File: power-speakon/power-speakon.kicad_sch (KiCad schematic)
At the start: 11 parts, among them J101 NL4MDXX-V-3, J102 NL4MDXX-V-3, J103 WAGO 2601-1101, J104 WAGO 2601-1101

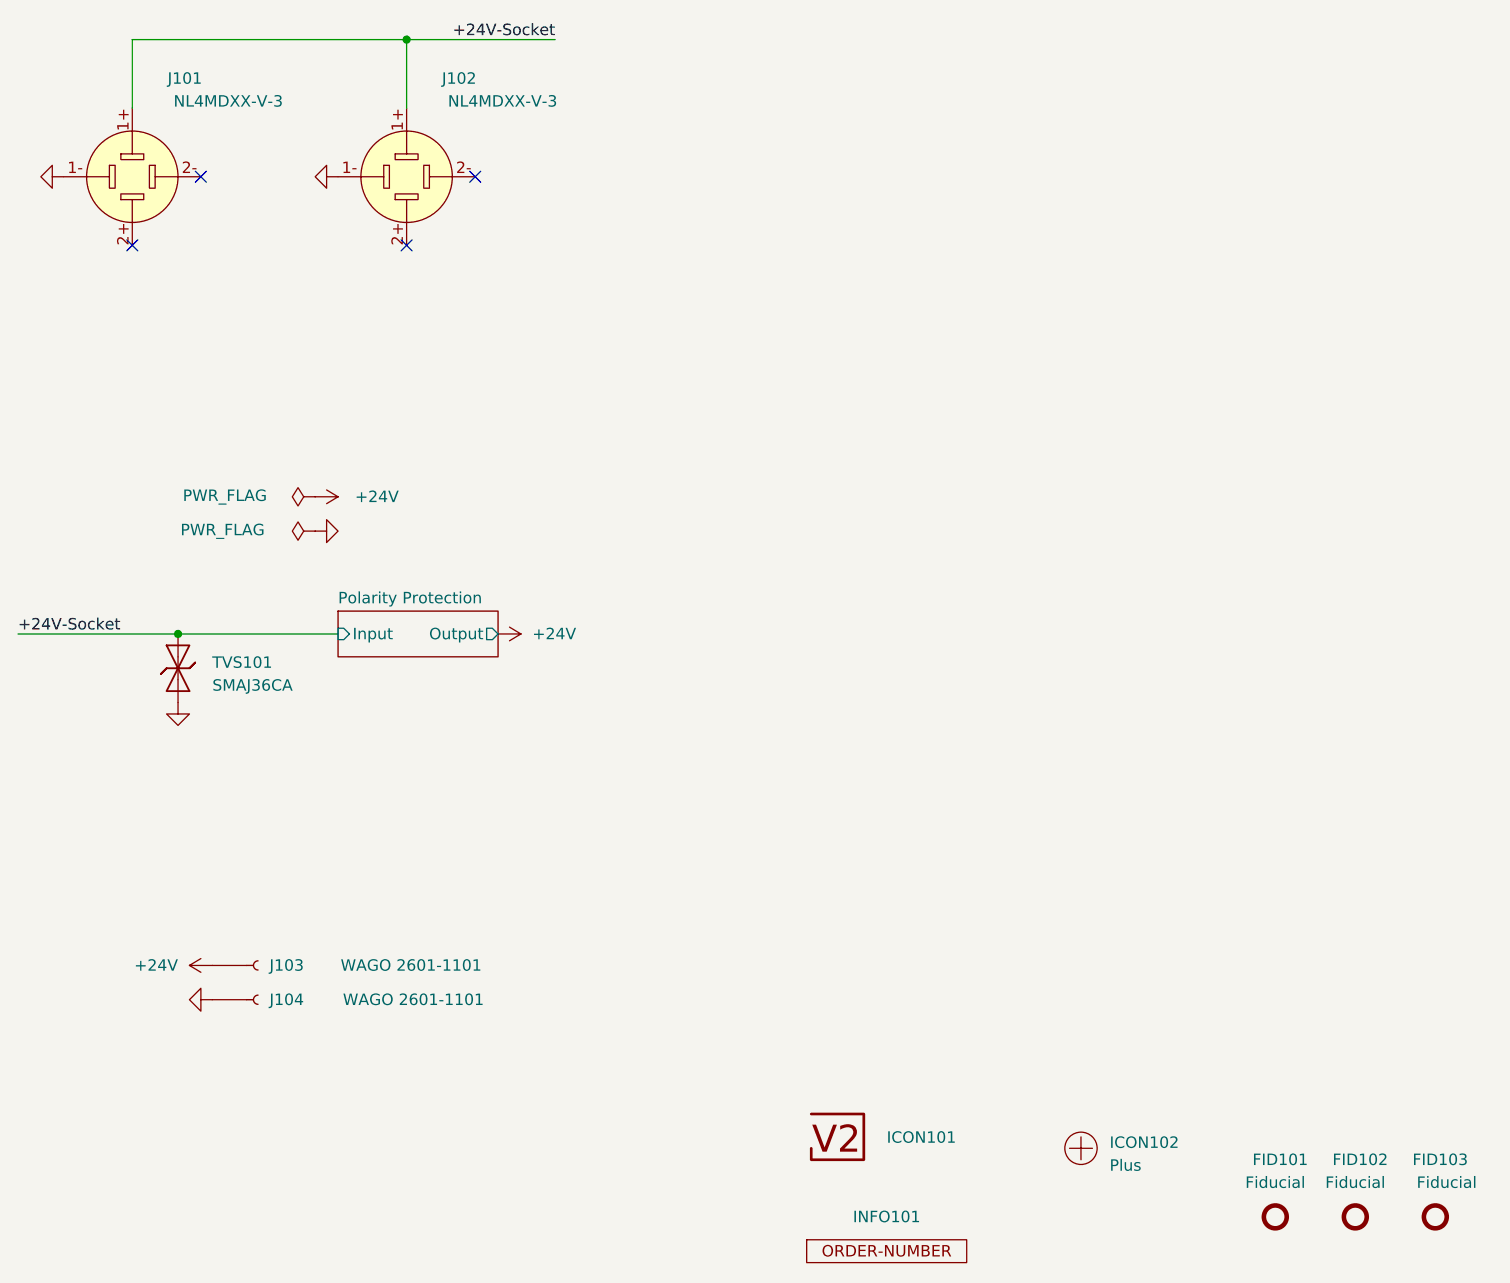
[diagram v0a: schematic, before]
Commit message: Update power symbols
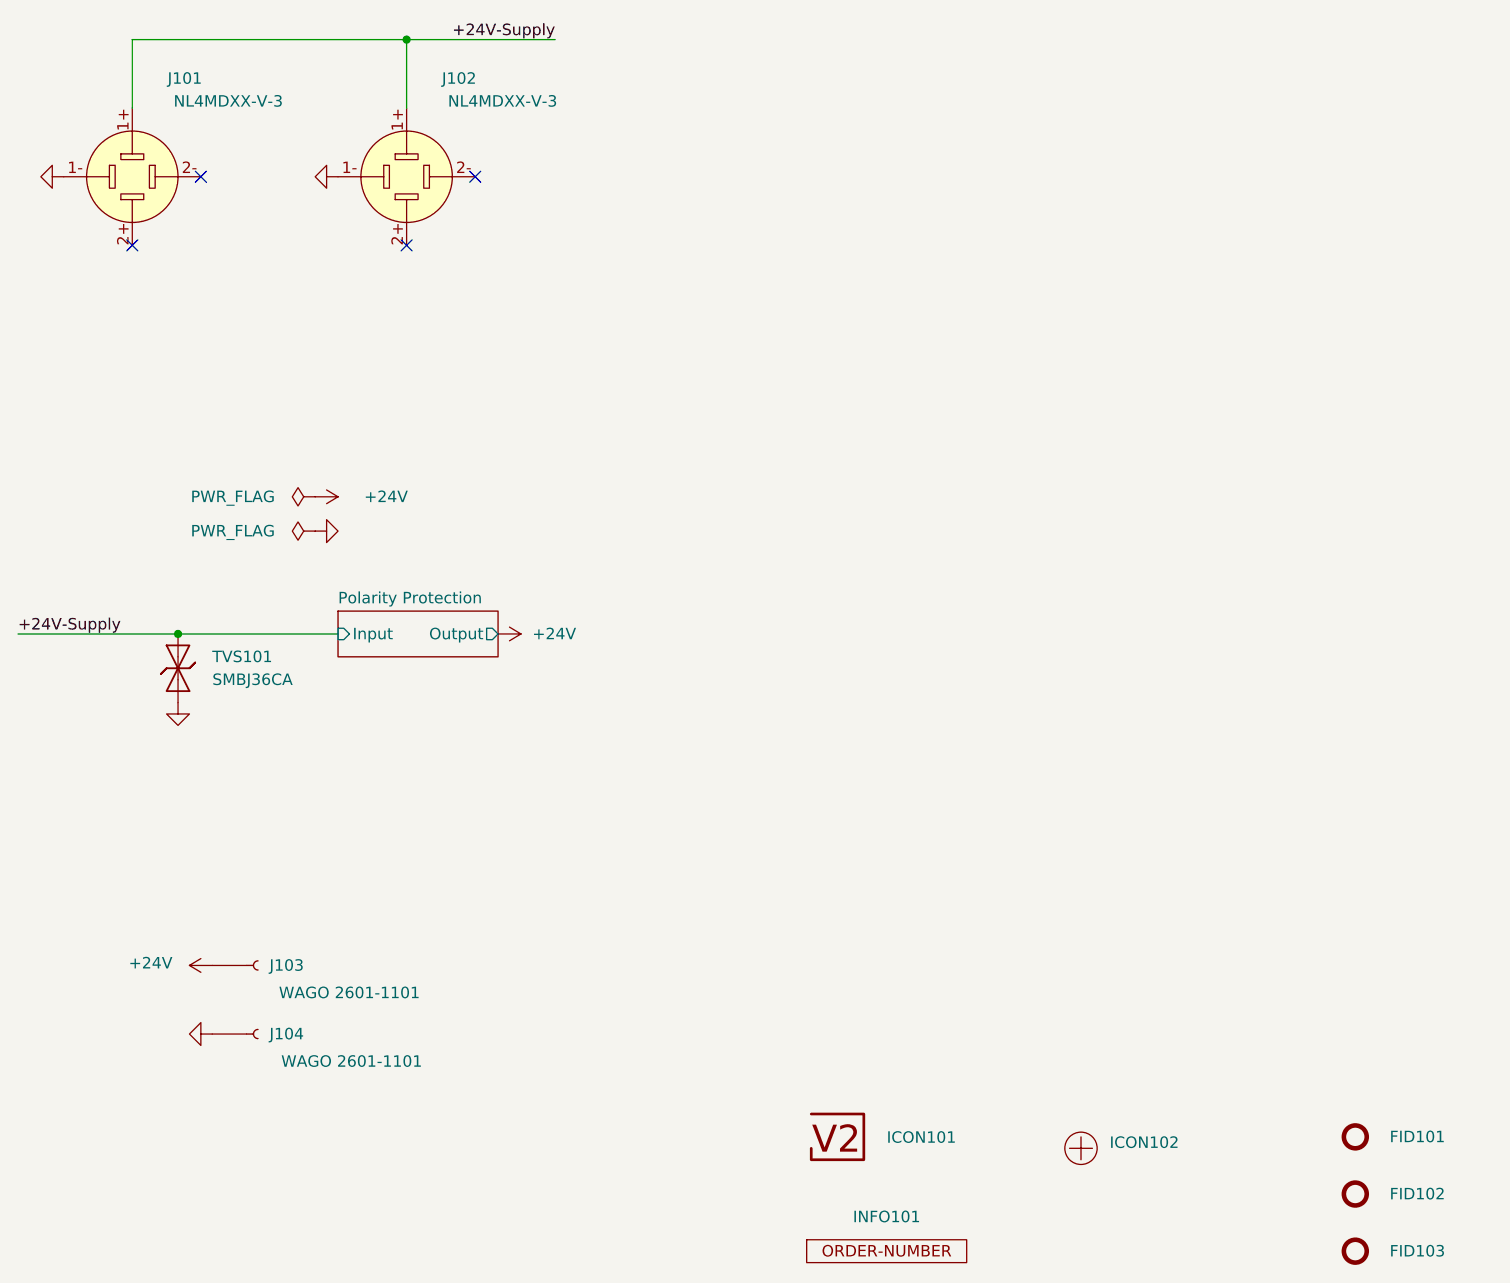
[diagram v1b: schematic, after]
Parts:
- FID101, FID102, FID103: value Fiducial -> Fiducial_Paste
- INFO101: value ORDER-NUMBER -> Order_Number
- J101, J102: Mouser (none) -> 568-NL4MDXXV3
- TVS101: value SMAJ36CA -> SMBJ36CA; footprint Diode_SMD:D_SMA -> V2_Diode_SMD:D_SMB; symbol V2_Diode:SMAJ36CA -> V2_Diode:SMBJ36CA; Mouser (none) -> 652-SMBJ36CA-Q
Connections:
- net +24V-Socket renamed +24V-Supply
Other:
- moved on the sheet: FID101, FID102, FID103, J104

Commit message: Update parts
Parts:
- J101, J102: Manufacturer (none) -> Neutrik; Product (none) -> NL4MDXXV3
- J103, J104: Manufacturer (none) -> WAGO; Product (none) -> 2601-1101
- TVS101: Manufacturer (none) -> Bourns; Product (none) -> SMBJ36CA-Q; Rating (none) -> 36V
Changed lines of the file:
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@@
+			)
+		)
+		(property "Product" "SMBJ36CA-Q"
+			(at 146.05 114.3 0)
+			(effects
+				(font
+					(size 1.27 1.27)
+				)
+				(hide yes)
+			)
+		)
+		(property "Manufacturer" "Bourns"
+			(at 143.51 114.3 0)
+			(effects
+				(font
+					(size 1.27 1.27)
+				)
+				(hide yes)
+			)
+		)
+		(property "Rating" "36V"
+			(at 148.59 114.3 0)
+			(effects
+				(font
+					(size 1.27 1.27)
+				)
+				(hide yes)
+			)
+		)
+		(property "Sim.Enable" ""
+			(at 135.89 114.3 90)
+			(effects
+				(font
+					(size 1.27 1.27)
+				)
+				(hide yes)
 			)
 		)
@@
 		(at 209.55 166.37 0)
 		(unit 1)
-		(exclude_from_sim no)
+		(exclude_from_sim yes)
 		(in_bom no)
 		(on_board yes)
@@
 			)
 		)
-		(property "Sim.Enable" "0"
+		(property "Sim.Enable" ""
 			(at 209.55 166.37 0)
 			(effects
@@
 			)
 		)
+		(property "Manufacturer" "WAGO"
+			(at 144.78 158.75 0)
+			(effects
+				(font
+					(size 1.27 1.27)
+				)
+				(hide yes)
+			)
+		)
+		(property "Product" "2601-1101"
+			(at 144.78 161.798 0)
+			(effects
+				(font
+					(size 1.27 1.27)
+				)
+				(hide yes)
+			)
+		)
+		(property "Sim.Enable" ""
+			(at 144.78 147.32 0)
+			(effects
+				(font
+					(size 1.27 1.27)
+				)
+				(hide yes)
+			)
+		)
 		(pin "1"
 		)
@@
 		(at 236.22 167.64 0)
 		(unit 1)
-		(exclude_from_sim no)
+		(exclude_from_sim yes)
 		(in_bom no)
 		(on_board yes)
@@
 			)
 		)
-		(property "Sim.Enable" "0"
+		(property "Sim.Enable" ""
 			(at 236.22 167.64 0)
 			(effects
@@
 			)
 		)
+		(property "Manufacturer" "Neutrik"
+			(at 161.29 87.63 0)
+			(effects
+				(font
+					(size 1.27 1.27)
+				)
+				(hide yes)
+			)
+		)
+		(property "Product" "NL4MDXXV3"
+			(at 161.29 90.17 0)
+			(effects
+				(font
+					(size 1.27 1.27)
+				)
+				(hide yes)
+			)
+		)
+		(property "Sim.Enable" ""
+			(at 161.29 59.69 0)
+			(effects
+				(font
+					(size 1.27 1.27)
+				)
+				(hide yes)
+			)
+		)
 		(pin "2-"
 		)
@@
 			)
 		)
+		(property "Sim.Enable" ""
+			(at 214.63 179.07 0)
+			(effects
+				(font
+					(size 1.27 1.27)
+				)
+				(hide yes)
+			)
+		)
 		(instances
 			(project "cube-cover"
@@
 			)
 		)
+		(property "Manufacturer" "WAGO"
+			(at 144.78 166.37 0)
+			(effects
+				(font
+					(size 1.27 1.27)
+				)
+				(hide yes)
+			)
+		)
+		(property "Product" "2601-1101"
+			(at 144.78 169.418 0)
+			(effects
+				(font
+					(size 1.27 1.27)
+				)
+				(hide yes)
+			)
+		)
+		(property "Sim.Enable" ""
+			(at 144.78 154.94 0)
+			(effects
+				(font
+					(size 1.27 1.27)
+				)
+				(hide yes)
+			)
+		)
 		(pin "1"
 		)
@@
 			)
 		)
+		(property "Sim.Enable" ""
+			(at 266.7 166.37 0)
+			(effects
+				(font
+					(size 1.27 1.27)
+				)
+				(hide yes)
+			)
+		)
 		(instances
 			(project "power-speakon"
@@
 			)
 		)
+		(property "Manufacturer" "Neutrik"
+			(at 130.81 87.63 0)
+			(effects
+				(font
+					(size 1.27 1.27)
+				)
+				(hide yes)
+			)
+		)
+		(property "Product" "NL4MDXXV3"
+			(at 130.81 90.17 0)
+			(effects
+				(font
+					(size 1.27 1.27)
+				)
+				(hide yes)
+			)
+		)
+		(property "Sim.Enable" ""
+			(at 130.81 59.69 0)
+			(effects
+				(font
+					(size 1.27 1.27)
+				)
+				(hide yes)
+			)
+		)
 		(pin "2-"
 		)
@@
 			)
 		)
+		(property "Sim.Enable" ""
+			(at 266.7 179.07 0)
+			(effects
+				(font
+					(size 1.27 1.27)
+				)
+				(hide yes)
+			)
+		)
 		(instances
 			(project "power-speakon"
@@
 			(at 266.7 172.72 0)
 			(effects
+				(font
+					(size 1.27 1.27)
+				)
+				(hide yes)
+			)
+		)
+		(property "Sim.Enable" ""
+			(at 266.7 172.72 0)
+			(effects

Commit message: Refresh
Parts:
- J101, J102: footprint V2_Connector_Audio:Jack_speakON_Neutrik_NL4MDXX-V-3_Vertical -> V2_Connector_SpeakOn:Jack_speakON_Neutrik_NL4MDXX-V-3_Vertical; symbol V2_Connector_Audio:NL4MDXX-V-3 -> V2_Connector_SpeakOn:NL4MDXX-V-3
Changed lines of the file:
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@@
-			)
-		)
-		(property "Sim.Enable" ""
-			(at 135.89 114.3 90)
-			(effects
-				(font
-					(size 1.27 1.27)
-				)
-				(hide yes)
 			)
 		)
@@
 		(at 209.55 166.37 0)
 		(unit 1)
-		(exclude_from_sim yes)
+		(exclude_from_sim no)
 		(in_bom no)
 		(on_board yes)
@@
 			)
 		)
-		(property "Sim.Enable" ""
+		(property "Sim.Enable" "0"
 			(at 209.55 166.37 0)
 			(effects
@@
 			)
 		)
-		(property "Sim.Enable" ""
-			(at 144.78 147.32 0)
-			(effects
-				(font
-					(size 1.27 1.27)
-				)
-				(hide yes)
-			)
-		)
 		(pin "1"
 		)
@@
 		(at 236.22 167.64 0)
 		(unit 1)
-		(exclude_from_sim yes)
+		(exclude_from_sim no)
 		(in_bom no)
 		(on_board yes)
@@
 			)
 		)
-		(property "Sim.Enable" ""
+		(property "Sim.Enable" "0"
 			(at 236.22 167.64 0)
 			(effects
@@
 	)
 	(symbol
-		(lib_id "V2_Connector_Audio:NL4MDXX-V-3")
+		(lib_id "V2_Connector_SpeakOn:NL4MDXX-V-3")
 		(at 161.29 59.69 0)
 		(unit 1)
@@
 			)
 		)
-		(property "Footprint" "V2_Connector_Audio:Jack_speakON_Neutrik_NL4MDXX-V-3_Vertical"
+		(property "Footprint" "V2_Connector_SpeakOn:Jack_speakON_Neutrik_NL4MDXX-V-3_Vertical"
 			(at 161.29 59.69 0)
 			(effects
@@
 			)
 		)
-		(property "Sim.Enable" ""
-			(at 161.29 59.69 0)
-			(effects
-				(font
-					(size 1.27 1.27)
-				)
-				(hide yes)
-			)
-		)
 		(pin "2-"
 		)
@@
 			)
 		)
-		(property "Sim.Enable" ""
-			(at 214.63 179.07 0)
-			(effects
-				(font
-					(size 1.27 1.27)
-				)
-				(hide yes)
-			)
-		)
 		(instances
 			(project "cube-cover"
@@
 			)
 		)
-		(property "Sim.Enable" ""
-			(at 144.78 154.94 0)
-			(effects
-				(font
-					(size 1.27 1.27)
-				)
-				(hide yes)
-			)
-		)
 		(pin "1"
 		)
@@
 			)
 		)
-		(property "Sim.Enable" ""
-			(at 266.7 166.37 0)
-			(effects
-				(font
-					(size 1.27 1.27)
-				)
-				(hide yes)
-			)
-		)
 		(instances
 			(project "power-speakon"
@@
 	)
 	(symbol
-		(lib_id "V2_Connector_Audio:NL4MDXX-V-3")
+		(lib_id "V2_Connector_SpeakOn:NL4MDXX-V-3")
 		(at 130.81 59.69 0)
 		(unit 1)
@@
 			)
 		)
-		(property "Footprint" "V2_Connector_Audio:Jack_speakON_Neutrik_NL4MDXX-V-3_Vertical"
+		(property "Footprint" "V2_Connector_SpeakOn:Jack_speakON_Neutrik_NL4MDXX-V-3_Vertical"
 			(at 130.81 59.69 0)
 			(effects
@@
 			)
 		)
-		(property "Sim.Enable" ""
-			(at 130.81 59.69 0)
-			(effects
-				(font
-					(size 1.27 1.27)
-				)
-				(hide yes)
-			)
-		)
 		(pin "2-"
 		)
@@
 			)
 		)
-		(property "Sim.Enable" ""
-			(at 266.7 179.07 0)
-			(effects
-				(font
-					(size 1.27 1.27)
-				)
-				(hide yes)
-			)
-		)
 		(instances
 			(project "power-speakon"
@@
 			(at 266.7 172.72 0)
 			(effects
-				(font
-					(size 1.27 1.27)
-				)
-				(hide yes)
-			)
-		)
-		(property "Sim.Enable" ""
-			(at 266.7 172.72 0)
-			(effects

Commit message: Update library
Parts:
- J101, J102: footprint V2_Connector_SpeakOn:Jack_speakON_Neutrik_NL4MDXX-V-3_Vertical -> V2_Connector_SpeakOn:NL4MDXX-V-3
- TVS101: value SMBJ36CA -> SMBJ33CA; symbol V2_Diode:SMBJ36CA -> V2_Diode:SMBJ33CA; Mouser 652-SMBJ36CA-Q -> 652-SMBJ33CA-Q; Product SMBJ36CA-Q -> SMBJ33CA-Q; Rating 36V -> 33V
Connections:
- net +24V renamed +28V
- net +24V-Supply renamed +28V-Supply
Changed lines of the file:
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@@
 		)
 	)
-	(label "+24V-Supply"
+	(label "+28V-Supply"
 		(at 177.8 44.45 180)
 		(effects
@@
 		)
 	)
-	(label "+24V-Supply"
+	(label "+28V-Supply"
 		(at 118.11 110.49 0)
 		(effects
@@
 			)
 		)
-		(property "Description" "Power symbol creates a global label with name \"GND\" , ground"
+		(property "Description" ""
 			(at 143.256 59.436 0)
 			(effects
@@
 			)
 		)
-		(property "Description" "Power symbol creates a global label with name \"GND\" , ground"
+		(property "Description" ""
 			(at 135.636 128.524 0)
 			(effects
@@
 	)
 	(symbol
-		(lib_id "V2_power:+24V")
+		(lib_id "V2_power:+28V")
 		(at 171.45 110.49 270)
 		(unit 1)
@@
 			)
 		)
-		(property "Value" "+24V"
+		(property "Value" "+28V"
 			(at 175.26 110.4899 90)
 			(effects
@@
 			)
 		)
-		(property "Description" "Power symbol creates a global label with name \"+24V\""
+		(property "Description" ""
 			(at 156.718 110.49 0)
 			(effects
@@
 	)
 	(symbol
-		(lib_id "V2_Diode:SMBJ36CA")
+		(lib_id "V2_Diode:SMBJ33CA")
 		(at 135.89 114.3 90)
 		(unit 1)
@@
 			)
 		)
-		(property "Value" "SMBJ36CA"
+		(property "Value" "SMBJ33CA"
 			(at 139.7 115.5699 90)
 			(effects
@@
 		)
 		(property "Datasheet" ""
-			(at 135.89 114.3 0)
-			(effects
-				(font
-					(size 1.27 1.27)
-				)
-				(hide yes)
-			)
-		)
-		(property "Description" ""
-			(at 135.89 114.3 0)
-			(effects
-				(font
-					(size 1.27 1.27)
-				)
-				(hide yes)
-			)
-		)
-		(property "Mouser" "652-SMBJ36CA-Q"
-			(at 143.256 114.3 0)
-			(effects
-				(font
-					(size 1.27 1.27)
-				)
-				(hide yes)
-			)
-		)
-		(property "Product" "SMBJ36CA-Q"
 			(at 146.05 114.3 0)
 			(effects
@@
 			)
 		)
+		(property "Description" "Transient Voltage Suppressor Diode, Bidirectional, 36.7-40.6V"
+			(at 148.59 114.3 0)
+			(effects
+				(font
+					(size 1.27 1.27)
+				)
+				(hide yes)
+			)
+		)
+		(property "Mouser" "652-SMBJ33CA-Q"
+			(at 159.004 114.3 0)
+			(show_name yes)
+			(effects
+				(font
+					(size 1.27 1.27)
+				)
+				(hide yes)
+			)
+		)
+		(property "Product" "SMBJ33CA-Q"
+			(at 153.67 114.3 0)
+			(show_name yes)
+			(effects
+				(font
+					(size 1.27 1.27)
+				)
+				(hide yes)
+			)
+		)
 		(property "Manufacturer" "Bourns"
-			(at 143.51 114.3 0)
-			(effects
-				(font
-					(size 1.27 1.27)
-				)
-				(hide yes)
-			)
-		)
-		(property "Rating" "36V"
-			(at 148.59 114.3 0)
+			(at 151.13 114.3 0)
+			(show_name yes)
+			(effects
+				(font
+					(size 1.27 1.27)
+				)
+				(hide yes)
+			)
+		)
+		(property "Rating" "33V"
+			(at 156.21 114.3 0)
+			(show_name yes)
 			(effects
 				(font
@@
 			)
 		)
-		(property "Description" "Power symbol creates a global label with name \"GND\" , ground"
+		(property "Description" ""
 			(at 161.544 99.314 0)
 			(effects
@@
 		(at 209.55 166.37 0)
 		(unit 1)
-		(exclude_from_sim no)
+		(exclude_from_sim yes)
 		(in_bom no)
 		(on_board yes)
@@
 	)
 	(symbol
-		(lib_id "V2_power:+24V")
+		(lib_id "V2_power:+28V")
 		(at 151.13 95.25 270)
 		(unit 1)
@@
 			)
 		)
-		(property "Value" "+24V"
+		(property "Value" "+28V"
 			(at 159.004 95.25 90)
 			(effects
@@
 			)
 		)
-		(property "Description" "Power symbol creates a global label with name \"+24V\""
+		(property "Description" ""
 			(at 136.398 95.25 0)
 			(effects
@@
 		(at 236.22 167.64 0)
 		(unit 1)
-		(exclude_from_sim no)
+		(exclude_from_sim yes)
 		(in_bom no)
 		(on_board yes)
@@
 			)
 		)
-		(property "Footprint" "V2_Connector_SpeakOn:Jack_speakON_Neutrik_NL4MDXX-V-3_Vertical"
+		(property "Footprint" "V2_Connector_SpeakOn:NL4MDXX-V-3"
 			(at 161.29 59.69 0)
 			(effects
@@
 	(symbol
 		(lib_id "V2_power:PWR_FLAG")
-		(at 151.13 99.06 90)
+		(at 151.13 99.06 0)
 		(unit 1)
 		(exclude_from_sim no)
@@
 		(dnp no)
 		(property "Reference" "#FLG0102"
-			(at 149.225 99.06 0)
+			(at 151.13 97.155 0)
 			(effects
 				(font
@@
 		)
 		(property "Value" "PWR_FLAG"
-			(at 141.986 99.06 90)
+			(at 141.224 99.06 0)
 			(effects
 				(font
@@
 		)
 		(property "Description" "Special symbol for telling ERC where power comes from"
-			(at 168.402 99.06 0)
+			(at 151.13 116.332 0)
 			(effects
 				(font
@@
 	(symbol
 		(lib_id "V2_power:PWR_FLAG")
-		(at 151.13 95.25 90)
+		(at 151.13 95.25 0)
 		(unit 1)
 		(exclude_from_sim no)
@@
 		(dnp no)
 		(property "Reference" "#FLG0101"
-			(at 149.225 95.25 0)
+			(at 151.13 93.345 0)
 			(effects
 				(font
@@
 		)
 		(property "Value" "PWR_FLAG"
-			(at 141.986 95.25 90)
+			(at 140.97 95.25 0)
 			(effects
 				(font
@@
 		)
 		(property "Description" "Special symbol for telling ERC where power comes from"
-			(at 168.402 95.25 0)
+			(at 151.13 112.522 0)
 			(effects
 				(font
@@
 			)
 		)
-		(property "Footprint" "V2_Connector_SpeakOn:Jack_speakON_Neutrik_NL4MDXX-V-3_Vertical"
+		(property "Footprint" "V2_Connector_SpeakOn:NL4MDXX-V-3"
 			(at 130.81 59.69 0)
 			(effects
@@
 	)
 	(symbol
-		(lib_id "V2_power:+24V")
+		(lib_id "V2_power:+28V")
 		(at 139.7 147.32 90)
 		(unit 1)
@@
 			)
 		)
-		(property "Value" "+24V"
+		(property "Value" "+28V"
 			(at 132.842 147.066 90)
 			(effects
@@
 			)
 		)
-		(property "Description" "Power symbol creates a global label with name \"+24V\""
+		(property "Description" ""
 			(at 154.432 147.32 0)
 			(effects
@@
 			)
 		)
-		(property "Description" "Power symbol creates a global label with name \"GND\" , ground"
+		(property "Description" ""
 			(at 129.286 154.686 0)
 			(effects
@@
 			)
 		)
-		(property "Description" "Power symbol creates a global label with name \"GND\" , ground"
+		(property "Description" ""
 			(at 112.776 59.436 0)
 			(effects
@@
 		(on_board yes)
 		(dnp no)
-		(fields_autoplaced yes)
 		(stroke
 			(width 0.1524)
@@
 		)
 		(property "Sheetname" "Polarity Protection"
-			(at 153.67 107.2384 0)
-			(effects
-				(font
+			(at 153.416 106.7304 0)
+			(effects
+				(font

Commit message: Replace Order_Number
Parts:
- INFO101: value Order_Number -> (none); footprint V2_Production:Order_Number -> V2_Production:Revision; symbol V2_Production:Order_Number -> V2_Production:Revision
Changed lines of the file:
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@@
-			)
-		)
-		(property "Sim.Enable" "0"
-			(at 209.55 166.37 0)
-			(effects
-				(font
-					(size 1.27 1.27)
-				)
-				(hide yes)
 			)
 		)
@@
 	)
 	(symbol
-		(lib_id "V2_Production:Order_Number")
+		(lib_id "V2_Production:Revision")
 		(at 214.63 179.07 0)
 		(unit 1)
@@
 			)
 		)
-		(property "Value" "Order_Number"
+		(property "Value" ""
 			(at 214.63 181.61 0)
 			(effects
@@
 			)
 		)
-		(property "Footprint" "V2_Production:Order_Number"
+		(property "Footprint" "V2_Production:Revision"
 			(at 214.63 184.15 0)
 			(effects
